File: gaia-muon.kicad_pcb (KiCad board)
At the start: 8 copper layers, 50 x 50 mm, 0 parts

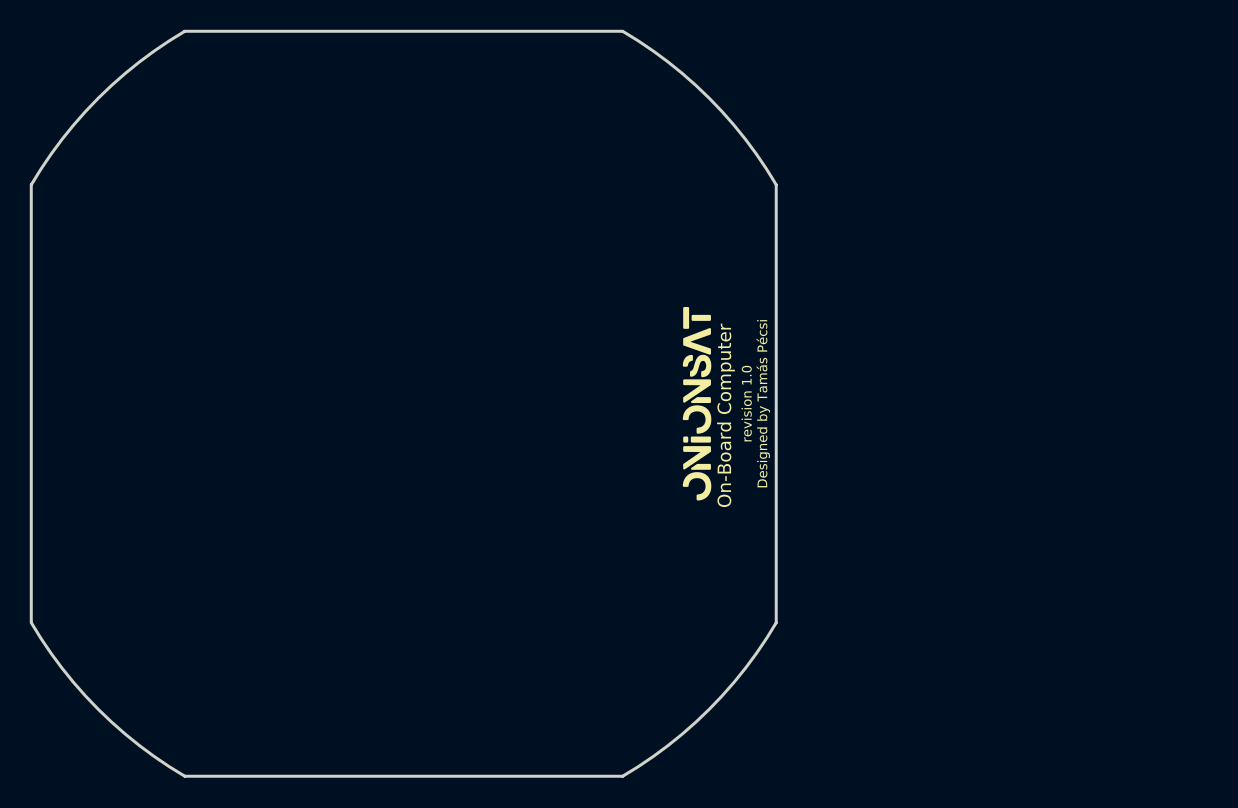
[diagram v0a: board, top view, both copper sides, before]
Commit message: placing components, start routing
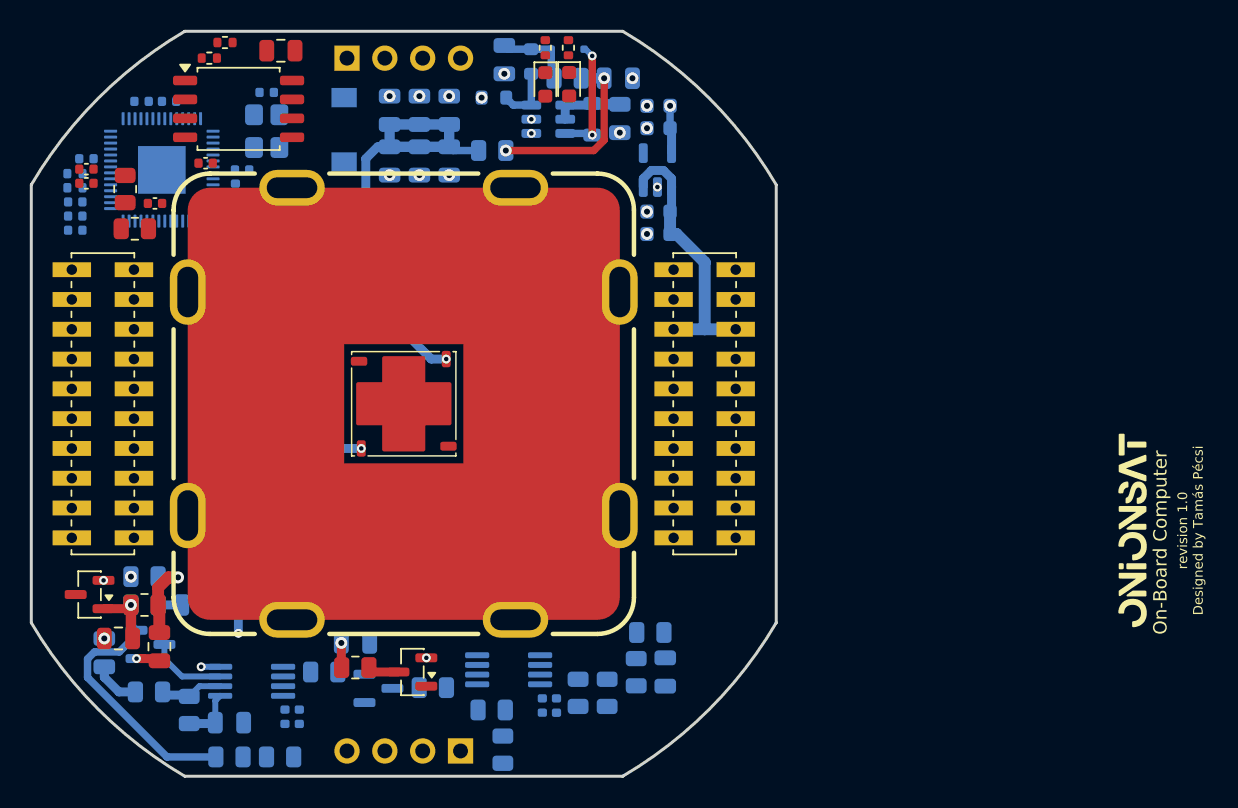
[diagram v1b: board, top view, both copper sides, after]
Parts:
- added C1: 1uF, Capacitor_SMD:C_0805_2012Metric, B.Cu at (151.1, 114.2)
- added C10: 200pF, Capacitor_SMD:C_0805_2012Metric, B.Cu at (161.8, 116.8)
- added C11: 1uF, Capacitor_SMD:C_0805_2012Metric, F.Cu at (148.6, 117.0)
- added C12: 100nF, Capacitor_SMD:C_0805_2012Metric, F.Cu at (145.8, 116.5)
- added C13: 100nF, Capacitor_SMD:C_0402_1005Metric, B.Cu at (175.2, 121.0)
- added C14: 4.7uF, Capacitor_SMD:C_0402_1005Metric, B.Cu at (174.3, 121.0)
- added C15: 100nF, Capacitor_SMD:C_0805_2012Metric, B.Cu at (168.1, 81.0)
- added C16: 100nF, Capacitor_SMD:C_0805_2012Metric, B.Cu at (168.1, 84.4)
- added C17: 10nF, Capacitor_SMD:C_0805_2012Metric, B.Cu at (166.1, 84.4)
- added C18: 10nF, Capacitor_SMD:C_0805_2012Metric, B.Cu at (166.1, 81.0)
- added C19: 10pF, Capacitor_SMD:C_0805_2012Metric, B.Cu at (164.1, 81.0)
- added C2: 1uF, Capacitor_SMD:C_0805_2012Metric, B.Cu at (144.9, 117.4)
- added C20: 10pF, Capacitor_SMD:C_0805_2012Metric, B.Cu at (164.1, 84.4)
- added C21: 100nF, Capacitor_SMD:C_0805_2012Metric, F.Cu at (156.8, 77.0)
- added C22: 15pF, Capacitor_SMD:C_0402_1005Metric, B.Cu at (155.8, 79.8)
- added C23: 15pF, Capacitor_SMD:C_0402_1005Metric, B.Cu at (154.2, 85.0)
- added C24: 1uF, Capacitor_SMD:C_0603_1608Metric, B.Cu at (182.1, 87.8)
- added C25: 100nF, Capacitor_SMD:C_0603_1608Metric, B.Cu at (182.1, 89.3)
- added C26: 1uF, Capacitor_SMD:C_0603_1608Metric, B.Cu at (182.1, 82.2)
- added C27: 100nF, Capacitor_SMD:C_0603_1608Metric, B.Cu at (182.1, 80.7)
- added C28: 100nF, Capacitor_SMD:C_0402_1005Metric, F.Cu at (143.7, 85.0)
- added C29: 100nF, Capacitor_SMD:C_0402_1005Metric, F.Cu at (143.7, 85.9)
- added C3: 1uF, Capacitor_SMD:C_0805_2012Metric, B.Cu at (171.8, 77.6)
- added C30: 100nF, Capacitor_SMD:C_0402_1005Metric, B.Cu at (149.2, 80.4)
- added C31: 100nF, Capacitor_SMD:C_0402_1005Metric, F.Cu at (148.3, 87.2)
- added C32: 100nF, Capacitor_SMD:C_0402_1005Metric, B.Cu at (143.7, 84.2)
- added C33: 100nF, Capacitor_SMD:C_0402_1005Metric, B.Cu at (147.4, 80.4)
- added C34: 100nF, Capacitor_SMD:C_0402_1005Metric, B.Cu at (142.9, 89.0)
- added C35: 100nF, Capacitor_SMD:C_0402_1005Metric, F.Cu at (151.7, 84.5)
- added C36: 1uF, Capacitor_SMD:C_0402_1005Metric, B.Cu at (142.9, 88.1)
- added C37: 100nF, Capacitor_SMD:C_0402_1005Metric, B.Cu at (153.7, 86.4)
- added C38: 1uF, Capacitor_SMD:C_0402_1005Metric, B.Cu at (142.9, 87.2)
- added C4: 4.7uF, Capacitor_SMD:C_0805_2012Metric, B.Cu at (179.5, 81.5)
- added C5: 1uF, Capacitor_SMD:C_0805_2012Metric, B.Cu at (179.4, 78.8)
- added C6: 100nF, Capacitor_SMD:C_0402_1005Metric, B.Cu at (158.0, 121.7)
- added C7: 4.7uF, Capacitor_SMD:C_0402_1005Metric, B.Cu at (157.0, 121.7)
- added C8: 1uF, Capacitor_SMD:C_0805_2012Metric, B.Cu at (153.3, 122.1)
- added C9: 1uF, Capacitor_SMD:C_0805_2012Metric, B.Cu at (182.6, 118.7)
- added D1: BAT54J, Diode_SMD:D_SOD-323F, B.Cu at (176.0, 76.9)
- added D2: BAT54S, Package_TO_SOT_SMD:SOT-23, B.Cu at (148.0, 116.8)
- added D3: BAT54S, Package_TO_SOT_SMD:SOT-23, B.Cu at (163.3, 119.8)
- added D4: LED_Small, LED_SMD:LED_0603_1608Metric, F.Cu at (176.1, 79.2)
- added D5: LED_Small, LED_SMD:LED_0603_1608Metric, F.Cu at (174.5, 79.3)
- added J1: Conn_02x10_Odd_Even, gaia-muon-footprints:Gaia_connector_2_4layer, F.Cu at (144.8, 100.7)
- added J2: Conn_02x10_Odd_Even, gaia-muon-footprints:Gaia_connector_2_4layer, F.Cu at (185.2, 100.7)
- added J3: Debug_Conn, Connector_PinHeader_2.54mm:PinHeader_1x04_P2.54mm_Vertical, B.Cu at (161.2, 77.5)
- added J4: Conn_01x04_Pin, Connector_PinHeader_2.54mm:PinHeader_1x04_P2.54mm_Vertical, B.Cu at (168.8, 124.0)
- added L1: 47uH, Inductor_SMD:L_0805_2012Metric, B.Cu at (177.7, 81.6)
- added Q1: 2N7002, Package_TO_SOT_SMD:SOT-23, F.Cu at (165.6, 118.7)
- added R1: 154k, Resistor_SMD:R_0603_1608Metric, B.Cu at (173.6, 77.7)
- added R10: 620, Resistor_SMD:R_0805_2012Metric, B.Cu at (150.6, 121.2)
- added R11: 1k, Resistor_SMD:R_0805_2012Metric, B.Cu at (181.6, 116.0)
- added R12: 1k, Resistor_SMD:R_0805_2012Metric, B.Cu at (180.6, 118.7)
- added R13: 1.3k, Resistor_SMD:R_0805_2012Metric, B.Cu at (171.7, 123.9)
- added R14: 1k, Resistor_SMD:R_0805_2012Metric, B.Cu at (170.9, 121.2)
- added R15: 1k, Resistor_SMD:R_0805_2012Metric, B.Cu at (156.7, 124.4)
- added R16: 100k, Resistor_SMD:R_0805_2012Metric, B.Cu at (153.3, 124.4)
- added R17: 0, Resistor_SMD:R_0805_2012Metric, B.Cu at (159.7, 118.7)
- added R18: 100, Resistor_SMD:R_0805_2012Metric, F.Cu at (147.6, 114.2)
- added R19: 100k, Resistor_SMD:R_0805_2012Metric, B.Cu at (166.9, 119.8)
- added R2: 6.65k, Resistor_SMD:R_0603_1608Metric, B.Cu at (171.1, 80.2)
- added R20: 10, Resistor_SMD:R_0805_2012Metric, B.Cu at (170.9, 83.7)
- added R21: TBA, Resistor_SMD:R_0402_1005Metric, F.Cu at (176.1, 76.8)
- added R22: TBA, Resistor_SMD:R_0402_1005Metric, F.Cu at (174.5, 76.8)
- added R23: DNF, Resistor_SMD:R_0402_1005Metric, F.Cu at (151.9, 77.5)
- added R24: 1k, Resistor_SMD:R_0402_1005Metric, F.Cu at (153.0, 76.5)
- added R25: 27, Resistor_SMD:R_0402_1005Metric, B.Cu at (142.9, 85.2)
- added R26: 27, Resistor_SMD:R_0402_1005Metric, B.Cu at (142.9, 86.2)
- added R27: 100, Resistor_SMD:R_0805_2012Metric, B.Cu at (153.0, 112.2)
- added R28: 22.1k, Resistor_SMD:R_0805_2012Metric, F.Cu at (146.9, 89.0)
- added R29: 1k, Resistor_SMD:R_0805_2012Metric, F.Cu at (146.3, 86.3)
- added R3: 1k, Resistor_SMD:R_0805_2012Metric, B.Cu at (176.7, 120.1)
- added R4: 1k, Resistor_SMD:R_0805_2012Metric, F.Cu at (161.8, 118.4)
- added R5: 2k, Resistor_SMD:R_0805_2012Metric, B.Cu at (178.7, 120.1)
- added R6: 1k, Resistor_SMD:R_0805_2012Metric, B.Cu at (147.6, 112.3)
- added R7: 100k, Resistor_SMD:R_0805_2012Metric, B.Cu at (147.6, 114.2)
- added R8: 49.9, Resistor_SMD:R_0805_2012Metric, B.Cu at (147.9, 120.0)
- added R9: 100, Resistor_SMD:R_0805_2012Metric, B.Cu at (176.0, 78.8)
- added SW1: SW_Push, gaia-muon-footprints:KEY-SMD_L4.0-W3.0-LS4.9-1, B.Cu at (161.0, 82.3)
- added U1: MAX5026, Package_TO_SOT_SMD:SOT-23-6, B.Cu at (174.7, 81.6)
- added U2: TPH2502, Package_SO:MSOP-8_3x3mm_P0.65mm, B.Cu at (172.0, 118.5)
- added U3: TPH2502, Package_SO:MSOP-8_3x3mm_P0.65mm, B.Cu at (154.8, 119.3)
- added U4: LM4040DBZ-2.5, Package_TO_SOT_SMD:SOT-23, F.Cu at (143.9, 113.5)
- added U5: W25Q128JVS, Package_SO:SOIC-8_5.3x5.3mm_P1.27mm, F.Cu at (153.9, 80.9)
- added U6: ~, gaia-muon-footprints:scintillator-case, F.Cu at (150.5, 86.2)
- added U7: MICROFC-60035-SIPM, gaia-muon-footprints:MICROFC-60035-SIPM, F.Cu at (165.0, 100.7)
- added U8: RP2040, Package_DFN_QFN:QFN-56-1EP_7x7mm_P0.4mm_EP3.2x3.2mm, B.Cu at (148.8, 85.0)
- added U9: AP2112K-3.3, Package_TO_SOT_SMD:SOT-23-5, B.Cu at (182.0, 85.0)
- added Y1: AMB8-272-T3, Crystal:Crystal_SMD_3225-4Pin_3.2x2.5mm, B.Cu at (155.8, 82.4)
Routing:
- net Net-(U7-CATHODE): track 0.00 -> 31.3 mm, vias 0 -> 1
- net VCC: track 0.00 -> 23.2 mm
- net VRef: track 0.00 -> 22.4 mm, vias 0 -> 1
- net SiPM: track 0.00 -> 18.8 mm, vias 0 -> 1
- net HV: track 0.00 -> 12.6 mm, vias 0 -> 2
- net Net-(D2-COM): track 0.00 -> 11.5 mm
- net Net-(D1-A): track 0.00 -> 7.91 mm, vias 0 -> 2
- net +3.3V: track 0.00 -> 7.82 mm, vias 0 -> 2
- net GND: track 0.00 -> 6.73 mm, vias 0 -> 24
- net Net-(D1-K): track 0.00 -> 5.28 mm
- net Net-(U3A--): track 0.00 -> 4.27 mm
- net Net-(U1-FB): track 0.00 -> 4.01 mm
- net Net-(C8-Pad1): track 0.00 -> 3.71 mm
- net Net-(C2-Pad2): track 0.00 -> 3.20 mm
- net Net-(Q1-D): track 0.00 -> 2.10 mm
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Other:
- board text added: "${REFERENCE}"

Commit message: finish routing
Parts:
- moved C37 0.15 mm to (153.8, 86.4)
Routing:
- net TriggerTresh: track 0.00 -> 60.4 mm, vias 0 -> 2
- net Trigger: track 0.00 -> 58.5 mm, vias 0 -> 1
- net Signal: track 0.00 -> 57.1 mm, vias 0 -> 2
- net PWM: track 0.00 -> 45.8 mm, vias 0 -> 2
- net TriggerReset: track 0.00 -> 43.8 mm, vias 0 -> 2
- net Amplifier: track 0.00 -> 39.1 mm, vias 0 -> 2
- net +1V1: track 0.00 -> 30.8 mm, vias 0 -> 2
- net /EXP0_USART_RXD: track 0.00 -> 30.5 mm, vias 0 -> 2
- net /EXP0_USART_TXD: track 0.00 -> 29.9 mm, vias 0 -> 2
- net /USB_DN: track 0.00 -> 29.1 mm, vias 0 -> 1
- net VRef: track 22.4 -> 51.3 mm, vias 1 -> 2
- net HV: track 12.6 -> 41.2 mm, vias 2 -> 4
- net VCC: track 23.2 -> 51.4 mm, vias 0 -> 2
- net /LED2: track 0.00 -> 25.8 mm, vias 0 -> 1
- net /USB_DP: track 0.00 -> 25.7 mm, vias 0 -> 1
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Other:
- board text added: "Muon Detector"
- board text added: "revision 1.0"
- board text removed: "${REFERENCE}"
- board text removed: "On-Board Computer"
- board text removed: "revision 1.0 Designed by Tamás Pécsi"
